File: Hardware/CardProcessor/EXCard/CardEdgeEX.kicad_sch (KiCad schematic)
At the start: 1 part, among them J1 MEC5-140-01-L-DV-W1-K

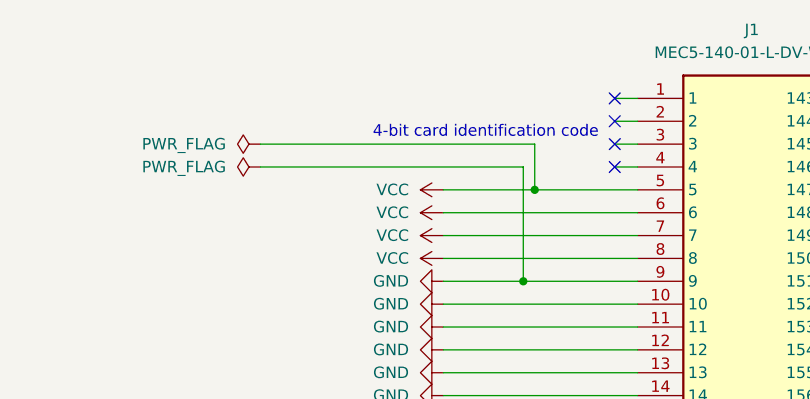
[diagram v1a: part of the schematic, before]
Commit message: Ensure all cards have a unique 4-bit identifier code and proper power pins
The pinout on all cards will devote the first four pins to the identifier,
followed by four pins for +5V, and four pins for GND. This allows a card to
draw up to about 2 amps.
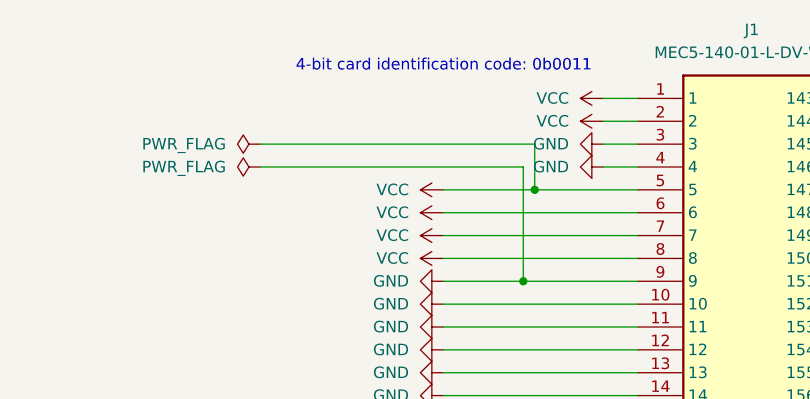
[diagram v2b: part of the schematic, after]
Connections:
- net GND: now also J1.3, J1.4
- net VCC: now also J1.1, J1.2
- no-connect marks 7 -> 3
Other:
- note added: "4-bit card identification code: 0b0011"
- note removed: "4-bit card identification code"
